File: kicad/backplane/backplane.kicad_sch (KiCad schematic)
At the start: 4 parts, among them J1 DIN41612_02x32_AC, J2 DIN41612_02x32_AC, J3 DIN41612_02x32_AC, J4 DIN41612_02x32_AC

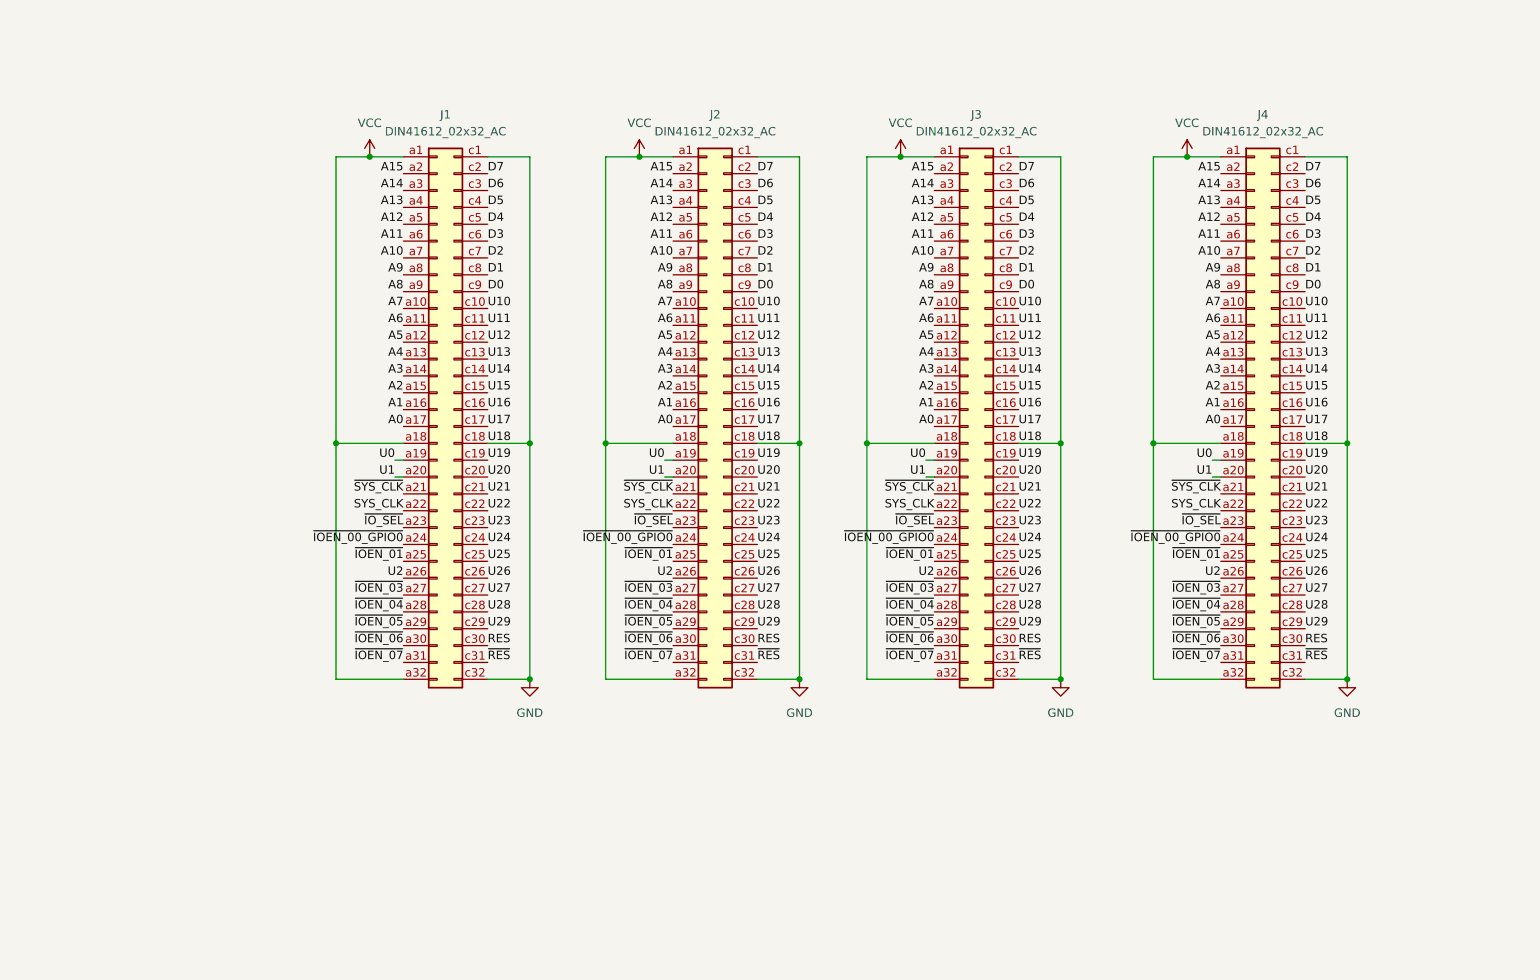
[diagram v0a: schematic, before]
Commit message: cpu board & backplane as ordered
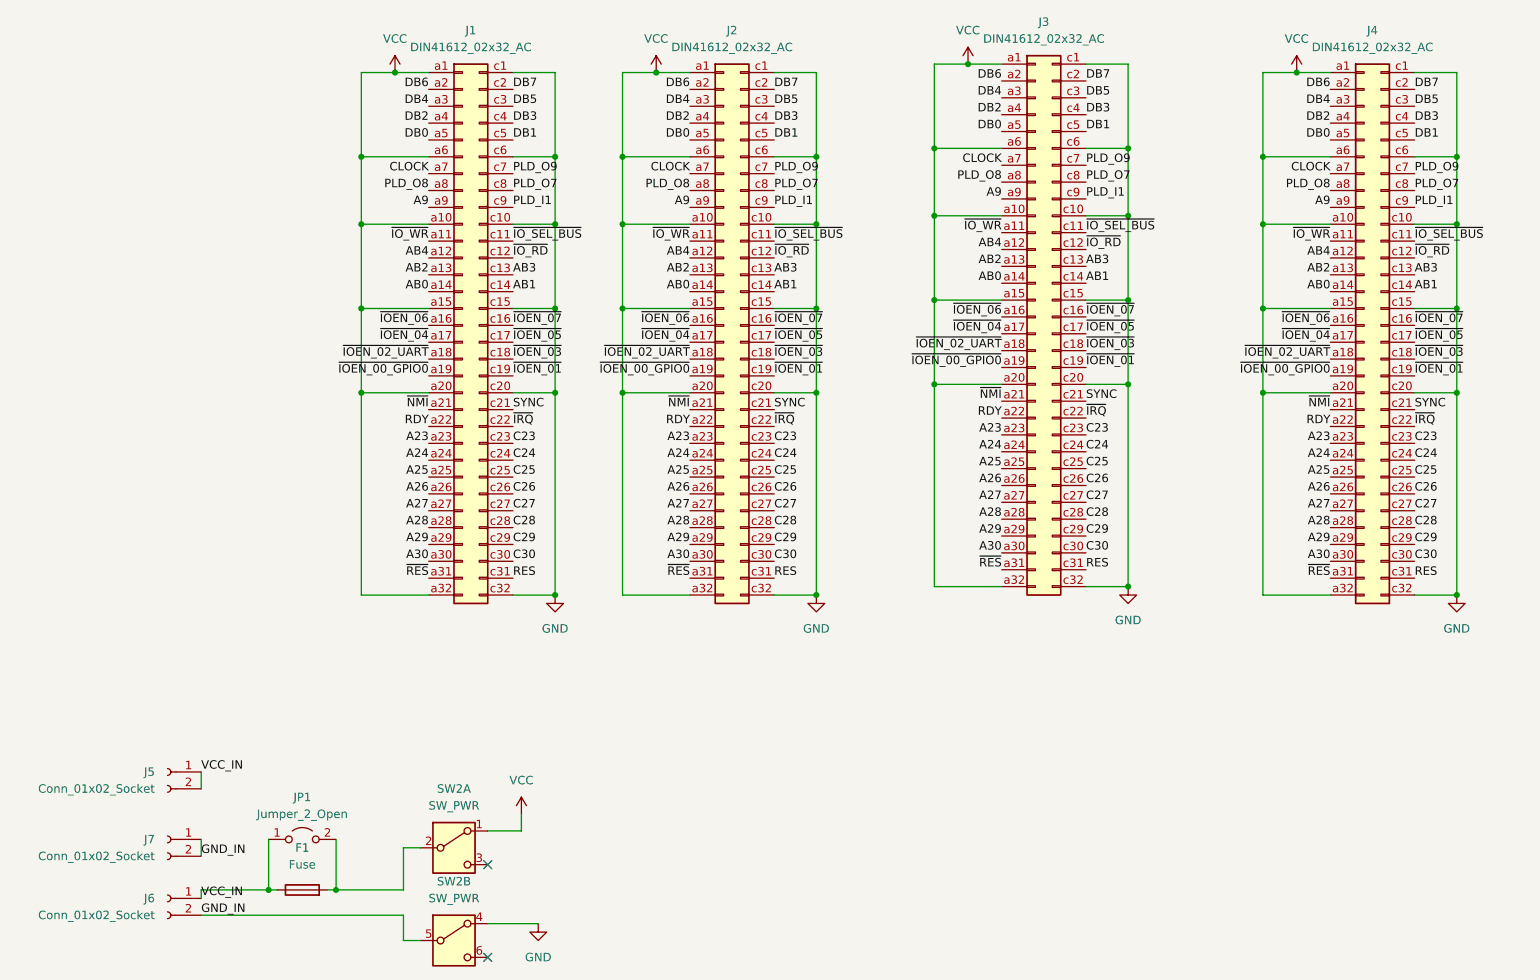
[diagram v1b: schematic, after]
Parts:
- added F1: Fuse, Fuse:Fuseholder_Cylinder-5x20mm_Stelvio-Kontek_PTF78_Horizontal_Open, symbol Device:Fuse
- added J5, J6, J7: Conn_01x02_Socket, Connector_PinSocket_2.54mm:PinSocket_1x02_P2.54mm_Vertical, symbol Connector:Conn_01x02_Socket
- added JP1: Jumper_2_Open, TestPoint:TestPoint_2Pads_Pitch2.54mm_Drill0.8mm, symbol Jumper:Jumper_2_Open
- added SW2: SW_PWR, sim82:7x7DPDT, symbol Switch:SW_DPDT_x2
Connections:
- net A0 is gone; now on net ~{IOEN_04}: J1.a17 (Pin_a17), J2.a17 (Pin_a17), J3.a17 (Pin_a17), J4.a17 (Pin_a17)
- net A1 is gone; now on net ~{IOEN_06}: J1.a16 (Pin_a16), J2.a16 (Pin_a16), J3.a16 (Pin_a16), J4.a16 (Pin_a16)
- net A11 is gone; now on net VCC: J1.a6 (Pin_a6), J2.a6 (Pin_a6), J3.a6 (Pin_a6), J4.a6 (Pin_a6)
- net A2 is gone; now on net VCC: J1.a15 (Pin_a15), J2.a15 (Pin_a15), J3.a15 (Pin_a15), J4.a15 (Pin_a15)
- net A7 is gone; now on net VCC: J1.a10 (Pin_a10), J2.a10 (Pin_a10), J3.a10 (Pin_a10), J4.a10 (Pin_a10)
- net A8 is gone; now on net A9: J1.a9 (Pin_a9), J2.a9 (Pin_a9), J3.a9 (Pin_a9), J4.a9 (Pin_a9)
- net D3 is gone; now on net GND: J1.c6 (Pin_c6), J2.c6 (Pin_c6), J3.c6 (Pin_c6), J4.c6 (Pin_c6)
- net U0 is gone; now on net ~{IOEN_00_GPIO0}: J1.a19 (Pin_a19), J2.a19 (Pin_a19), J3.a19 (Pin_a19), J4.a19 (Pin_a19)
- net U1 is gone; now on net VCC: J1.a20 (Pin_a20), J2.a20 (Pin_a20), J3.a20 (Pin_a20), J4.a20 (Pin_a20)
- net U10 is gone; now on net GND: J1.c10 (Pin_c10), J2.c10 (Pin_c10), J3.c10 (Pin_c10), J4.c10 (Pin_c10)
- net U15 is gone; now on net GND: J1.c15 (Pin_c15), J2.c15 (Pin_c15), J3.c15 (Pin_c15), J4.c15 (Pin_c15)
- net U16 is gone; now on net ~{IOEN_07}: J1.c16 (Pin_c16), J2.c16 (Pin_c16), J3.c16 (Pin_c16), J4.c16 (Pin_c16)
- net U17 is gone; now on net ~{IOEN_05}: J1.c17 (Pin_c17), J2.c17 (Pin_c17), J3.c17 (Pin_c17), J4.c17 (Pin_c17)
- net U19 is gone; now on net ~{IOEN_01}: J1.c19 (Pin_c19), J2.c19 (Pin_c19), J3.c19 (Pin_c19), J4.c19 (Pin_c19)
- net U20 is gone; now on net GND: J1.c20 (Pin_c20), J2.c20 (Pin_c20), J3.c20 (Pin_c20), J4.c20 (Pin_c20)
- net A9: no longer J1.a8 (Pin_a8), J2.a8 (Pin_a8), J3.a8 (Pin_a8), J4.a8 (Pin_a8)
- net GND: now also SW2.4 (A); no longer J1.c18 (Pin_c18), J2.c18 (Pin_c18), J3.c18 (Pin_c18), J4.c18 (Pin_c18)
- net RES: now also J1.c31 (Pin_c31), J2.c31 (Pin_c31), J3.c31 (Pin_c31), J4.c31 (Pin_c31); no longer J1.c30 (Pin_c30), J2.c30 (Pin_c30), J3.c30 (Pin_c30), J4.c30 (Pin_c30)
- net VCC: now also SW2.1 (A); no longer J1.a18 (Pin_a18), J2.a18 (Pin_a18), J3.a18 (Pin_a18), J4.a18 (Pin_a18)
- net ~{IOEN_00_GPIO0}: no longer J1.a24 (Pin_a24), J2.a24 (Pin_a24), J3.a24 (Pin_a24), J4.a24 (Pin_a24)
- net ~{IOEN_01}: no longer J1.a25 (Pin_a25), J2.a25 (Pin_a25), J3.a25 (Pin_a25), J4.a25 (Pin_a25)
- net ~{IOEN_03}: now also J1.c18 (Pin_c18), J2.c18 (Pin_c18), J3.c18 (Pin_c18), J4.c18 (Pin_c18); no longer J1.a27 (Pin_a27), J2.a27 (Pin_a27), J3.a27 (Pin_a27), J4.a27 (Pin_a27)
- net ~{IOEN_04}: no longer J1.a28 (Pin_a28), J2.a28 (Pin_a28), J3.a28 (Pin_a28), J4.a28 (Pin_a28)
- net ~{IOEN_05}: no longer J1.a29 (Pin_a29), J2.a29 (Pin_a29), J3.a29 (Pin_a29), J4.a29 (Pin_a29)
- net ~{IOEN_06}: no longer J1.a30 (Pin_a30), J2.a30 (Pin_a30), J3.a30 (Pin_a30), J4.a30 (Pin_a30)
- net ~{IOEN_07}: no longer J1.a31 (Pin_a31), J2.a31 (Pin_a31), J3.a31 (Pin_a31), J4.a31 (Pin_a31)
- net ~{RES}: now also J1.a31 (Pin_a31), J2.a31 (Pin_a31), J3.a31 (Pin_a31), J4.a31 (Pin_a31); no longer J1.c31 (Pin_c31), J2.c31 (Pin_c31), J3.c31 (Pin_c31), J4.c31 (Pin_c31)
- net A10 renamed CLOCK
- net A12 renamed DB0
- net A13 renamed DB2
- net A14 renamed DB4
- net A15 renamed DB6
- net A3 renamed AB0
- net A4 renamed AB2
- net A5 renamed AB4
- net A6 renamed ~{IO_WR}
- net D0 renamed PLD_I1
- net D1 renamed PLD_O7
- net D2 renamed PLD_O9
- net D4 renamed DB1
- net D5 renamed DB3
- net D6 renamed DB5
- net D7 renamed DB7
- net SYS_CLK renamed RDY
- net U11 renamed ~{IO_SEL_BUS}
- net U12 renamed ~{IO_RD}
- net U13 renamed AB3
- net U14 renamed AB1
- net U2 renamed A26
- net U21 renamed SYNC
- net U22 renamed ~{IRQ}
- net U23 renamed C23
- net U24 renamed C24
- net U25 renamed C25
- net U26 renamed C26
- net U27 renamed C27
- net U28 renamed C28
- net U29 renamed C29
- net ~{IO_SEL} renamed A23
- net ~{SYS_CLK} renamed ~{NMI}
- new net: F1.2, JP1.2 (B), SW2.2 (B)
- new net A24: J1.a24 (Pin_a24), J2.a24 (Pin_a24), J3.a24 (Pin_a24), J4.a24 (Pin_a24)
- new net A25: J1.a25 (Pin_a25), J2.a25 (Pin_a25), J3.a25 (Pin_a25), J4.a25 (Pin_a25)
- new net A27: J1.a27 (Pin_a27), J2.a27 (Pin_a27), J3.a27 (Pin_a27), J4.a27 (Pin_a27)
- new net A28: J1.a28 (Pin_a28), J2.a28 (Pin_a28), J3.a28 (Pin_a28), J4.a28 (Pin_a28)
- new net A29: J1.a29 (Pin_a29), J2.a29 (Pin_a29), J3.a29 (Pin_a29), J4.a29 (Pin_a29)
- new net A30: J1.a30 (Pin_a30), J2.a30 (Pin_a30), J3.a30 (Pin_a30), J4.a30 (Pin_a30)
- new net C30: J1.c30 (Pin_c30), J2.c30 (Pin_c30), J3.c30 (Pin_c30), J4.c30 (Pin_c30)
- new net GND_IN: J6.2 (Pin_2), J7.1 (Pin_1), J7.2 (Pin_2), SW2.5 (B)
- new net PLD_O8: J1.a8 (Pin_a8), J2.a8 (Pin_a8), J3.a8 (Pin_a8), J4.a8 (Pin_a8)
- new net VCC_IN: F1.1, J5.1 (Pin_1), J5.2 (Pin_2), J6.1 (Pin_1), JP1.1 (A)
- new net ~{IOEN_02_UART}: J1.a18 (Pin_a18), J2.a18 (Pin_a18), J3.a18 (Pin_a18), J4.a18 (Pin_a18)
- no-connect marks 0 -> 2
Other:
- moved on the sheet: J1
